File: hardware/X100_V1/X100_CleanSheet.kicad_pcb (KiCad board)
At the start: 4 copper layers, 45 x 45 mm, 205 parts, among them J401 124019772112A, J501 1040310811, J601 SM04B-GHS-TB(LF)(SN), J701 SM06B-GHS-TB(LF)(SN), J702 SM06B-GHS-TB(LF)(SN), J703 SM06B-GHS-TB(LF)(SN), J704 SM04B-GHS-TB(LF)(SN), J801 OUT1 /GND, J802 OUT2 /GND, J803 OUT3 /GND, J804 OUT4 /GND, J805 OUT5 /GND, J806 OUT6 /GND, J807 SWD:1REF2GND3IO4CLK5NRST, J808 BATTERY/bench3S-6S ONLY, J809 CURRENT monitor only, Q101 DMP6023LSS-13, U101 TPS54360BDDAR, U102 AP63203WU-7, U103 TPS7A2033PDBVR, U104 TPS2553DBVR, U201 STM32H743VIT6, U301 BMI088, U302 SPL06-001, U401 TPD2E2U06QDBZRQ1, U402 SN74LVC1G17DBVR, U403 TPD2E2U06QDBZRQ1, U404 TPD2E2U06QDBZRQ1, U601 TCAN3414DR, U801 TMUX1511PWR, Y201 8.000MHz /CL20pF

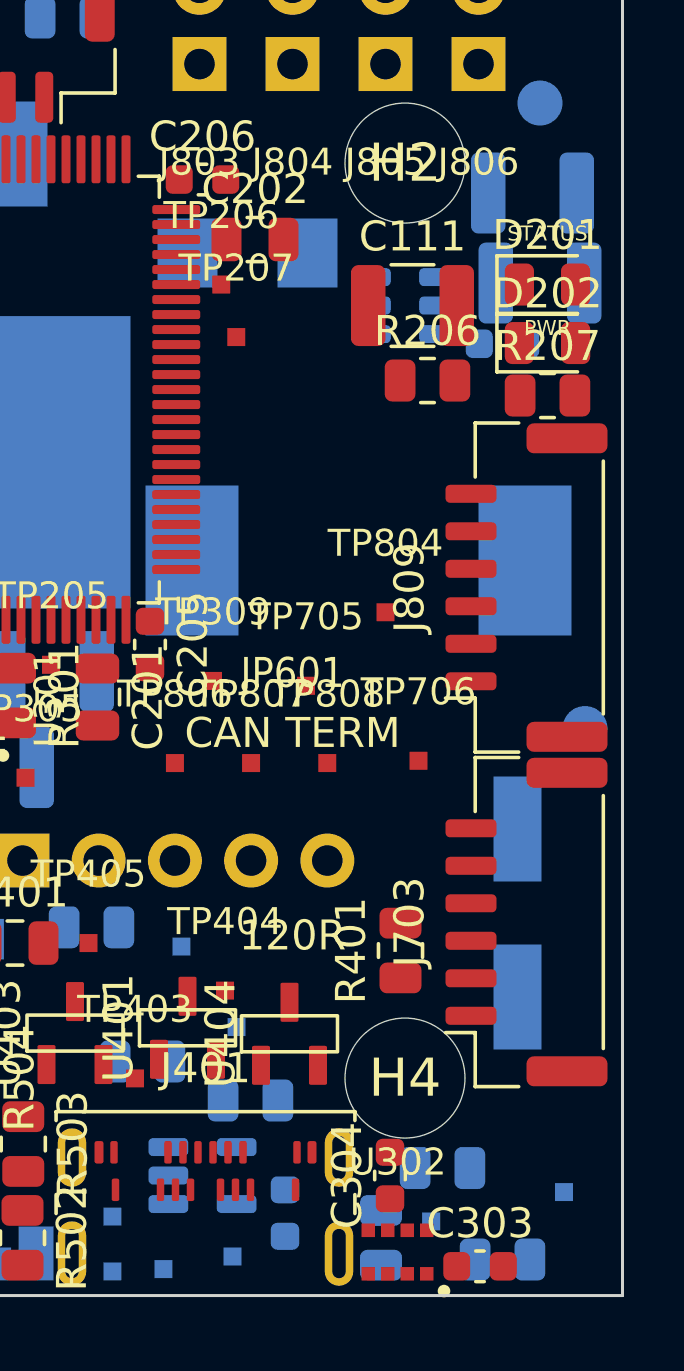
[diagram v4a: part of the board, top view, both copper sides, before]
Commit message: 关闭右侧接口间及J703安装孔净空冲突
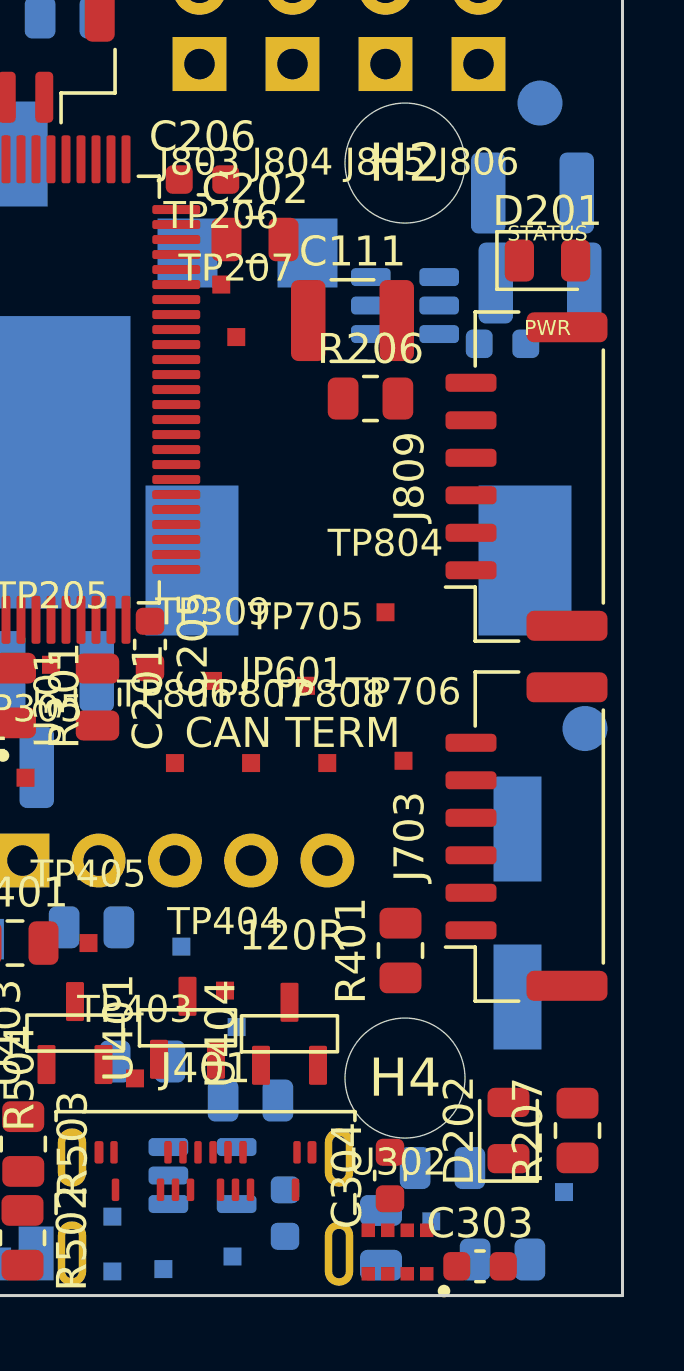
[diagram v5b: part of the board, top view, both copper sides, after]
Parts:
- moved D202 26.3 mm to (118.7, 117.0), turned to 90 degrees
- moved R207 24.5 mm to (121.0, 117.0), turned to 90 degrees
- moved J809 3.70 mm to (119.3, 95.2)
- moved J703 2.85 mm to (119.3, 107.2)
- moved C111 2.06 mm to (113.5, 90.0)
- moved R206 1.99 mm to (114.1, 92.6)
- moved D201 0.80 mm to (120.0, 88.0)
- moved TP706 0.50 mm to (115.2, 104.7)
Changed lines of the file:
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@@
 	(footprint "X100_Physical:Official_LED_SMD_LED_0805_2012Metric"
 		(layer "F.Cu")
-		(at 120 88.8)
+		(at 120 88)
 		(descr "LED SMD 0805 (2012 Metric), square (rectangular) end terminal, IPC-7351 nominal, (Body size source: https://docs.google.com/spreadsheets/d/1BsfQQcO9C6DZCsRaXUlFlo91Tg2WpOkGARC1WS5S8t0/edit?usp=sharing)")
 		(tags "LED")
@@
 	(footprint "X100_Physical:Official_Capacitor_SMD_C_1210_3225Metric"
 		(layer "F.Cu")
-		(at 115.5 89.5)
+		(at 113.5 90)
 		(descr "Capacitor SMD 1210 (3225 Metric), square (rectangular) end terminal, IPC-7351 nominal, (Body size source: IPC-SM-782 page 76, https://www.pcb-3d.com/wordpress/wp-content/uploads/ipc-sm-782a_amendment_1_and_2.pdf)")
 		(tags "capacitor")
@@
 	(footprint "X100_Physical:TP0p6_Inline_NoPaste"
 		(layer "F.Cu")
-		(at 115.7 104.675)
+		(at 115.2 104.675)
 		(descr "Project0.6mm inline probe pad; high speed no long branch; no hole; no paste")
 		(property "Reference" "TP706"
@@
 	(footprint "X100_Physical:Official_Resistor_SMD_R_0805_2012Metric"
 		(layer "F.Cu")
-		(at 120 92.5)
+		(at 121 117 90)
 		(descr "Resistor SMD 0805 (2012 Metric), square (rectangular) end terminal, IPC-7351 nominal, (Body size source: IPC-SM-782 page 72, https://www.pcb-3d.com/wordpress/wp-content/uploads/ipc-sm-782a_amendment_1_and_2.pdf)")
 		(tags "resistor")
 		(property "Reference" "R207"
-			(at 0 -1.65 0)
+			(at 0 -1.65 90)
 			(layer "F.SilkS")
 			(effects
@@
 		)
 		(property "Value" "1.2k PWR current"
-			(at 0 1.65 0)
+			(at 0 1.65 90)
 			(layer "F.Fab")
 			(effects
@@
 		)
 		(property "Datasheet" "https://www.yageogroup.com/component-documentation/download/specsheet/RC0805FR-071K2L"
-			(at 0 0 0)
+			(at 0 0 90)
 			(layer "F.Fab")
 			(hide yes)
@@
 		)
 		(property "Description" ""
-			(at 0 0 0)
+			(at 0 0 90)
 			(layer "F.Fab")
 			(hide yes)
@@
 		)
 		(property "KiLib_Generator" "SMD_2terminal_chip_molded"
-			(at 0 0 0)
+			(at 0 0 90)
 			(layer "F.SilkS")
 			(hide yes)
@@
 		)
 		(property "Manufacturer" "YAGEO"
-			(at 0 0 0)
+			(at 0 0 90)
 			(layer "F.Fab")
 			(hide yes)
@@
 		)
 		(property "MPN" "RC0805FR-071K2L"
-			(at 0 0 0)
+			(at 0 0 90)
 			(layer "F.Fab")
 			(hide yes)
@@
 		)
 		(property "Package" "0805"
-			(at 0 0 0)
+			(at 0 0 90)
 			(layer "F.Fab")
 			(hide yes)
@@
 		)
 		(property "Procurement Policy" "SPECIFICATION_FROZEN_PREFERRED_BOM; PCB01F3 prototype 1.2k authorized"
-			(at 0 0 0)
+			(at 0 0 90)
 			(layer "F.Fab")
 			(hide yes)
@@
 		)
 		(property "Specification Value" "1.2k ohm"
-			(at 0 0 0)
+			(at 0 0 90)
 			(layer "F.Fab")
 			(hide yes)
@@
 		)
 		(property "Tolerance" "1%; TCR<=100ppm/C"
-			(at 0 0 0)
+			(at 0 0 90)
 			(layer "F.Fab")
 			(hide yes)
@@
 		)
 		(property "Dielectric" "N/A"
-			(at 0 0 0)
+			(at 0 0 90)
 			(layer "F.Fab")
 			(hide yes)
@@
 		)
 		(property "Voltage Rating" ">=100V"
-			(at 0 0 0)
+			(at 0 0 90)
 			(layer "F.Fab")
 			(hide yes)
@@
 		)
 		(property "Power Rating" ">=0.125W"
-			(at 0 0 0)
+			(at 0 0 90)
 			(layer "F.Fab")
 			(hide yes)
@@
 		)
 		(property "LCSC" "C114526"
-			(at 0 0 0)
+			(at 0 0 90)
 			(layer "F.Fab")
 			(hide yes)
@@
 		)
 		(fp_text user "${REFERENCE}"
-			(at 0 0 0)
+			(at 0 0 90)
 			(layer "F.Fab")
 			(effects
@@
 		)
 		(pad "1" smd roundrect
-			(at -0.9125 0)
+			(at -0.9125 0 90)
 			(size 1.025 1.4)
 			(layers "F.Cu" "F.Mask" "F.Paste")
@@
 		)
 		(pad "2" smd roundrect
-			(at 0.9125 0)
+			(at 0.9125 0 90)
 			(size 1.025 1.4)
 			(layers "F.Cu" "F.Mask" "F.Paste")
@@
 	(footprint "X100_Physical:Official_Connector_JST_JST_GH_SM06B-GHS-TB_1x06-1MP_P1.25mm_Horizontal"
 		(layer "F.Cu")
-		(at 119.3 98.899999 90)
+		(at 119.3 95.2 90)
 		(descr "JST GH series connector, SM06B-GHS-TB (http://www.jst-mfg.com/product/pdf/eng/eGH.pdf)")
 		(tags "connector JST GH horizontal")
@@
 	(footprint "X100_Physical:Official_Connector_JST_JST_GH_SM06B-GHS-TB_1x06-1MP_P1.25mm_Horizontal"
 		(layer "F.Cu")
-		(at 119.3 110.05 90)
+		(at 119.3 107.2 90)
 		(descr "JST GH series connector, SM06B-GHS-TB (http://www.jst-mfg.com/product/pdf/eng/eGH.pdf)")
 		(tags "connector JST GH horizontal")
@@
 	(footprint "X100_Physical:Official_LED_SMD_LED_0805_2012Metric"
 		(layer "F.Cu")
-		(at 120 90.75)
+		(at 118.7 117 90)
 		(descr "LED SMD 0805 (2012 Metric), square (rectangular) end terminal, IPC-7351 nominal, (Body size source: https://docs.google.com/spreadsheets/d/1BsfQQcO9C6DZCsRaXUlFlo91Tg2WpOkGARC1WS5S8t0/edit?usp=sharing)")
 		(tags "LED")
 		(property "Reference" "D202"
-			(at 0 -1.65 0)
+			(at 0 -1.65 90)
 			(layer "F.SilkS")
 			(effects
@@
 		)
 		(property "Value" "GREEN; 3V3_MCU_PRESENT"
-			(at 0 1.65 0)
+			(at 0 1.65 90)
 			(layer "F.Fab")
 			(effects
@@
 		)
 		(property "Datasheet" "https://optoelectronics.liteon.com/upload/download/DS22-2000-003/LTST-C170GKT.pdf"
-			(at 0 0 0)
+			(at 0 0 90)
 			(layer "F.Fab")
 			(hide yes)
@@
 		)
 		(property "Description" ""
-			(at 0 0 0)
+			(at 0 0 90)
 			(layer "F.Fab")
 			(hide yes)
@@
 		)
 		(property "KiLib_Generator" "SMD_2terminal_chip_molded"
-			(at 0 0 0)
+			(at 0 0 90)
 			(layer "F.SilkS")
 			(hide yes)
@@
 		)
 		(property "Manufacturer" "Lite-On"
-			(at 0 0 0)
+			(at 0 0 90)
 			(layer "F.Fab")
 			(hide yes)
@@
 		)
 		(property "MPN" "LTST-C170GKT"
-			(at 0 0 0)
+			(at 0 0 90)
 			(layer "F.Fab")
 			(hide yes)
@@
 		)
 		(property "Package" "0805 LED"
-			(at 0 0 0)
+			(at 0 0 90)
 			(layer "F.Fab")
 			(hide yes)
@@
 		)
 		(property "Procurement Policy" "EXACT_MPN_AUTHORIZED_PCB01F3; same LED as D201; not ordered"
-			(at 0 0 0)
+			(at 0 0 90)
 			(layer "F.Fab")
 			(hide yes)
@@
 		)
 		(property "LCSC" "C125090"
-			(at 0 0 0)
+			(at 0 0 90)
 			(layer "F.Fab")
 			(hide yes)
@@
 		(duplicate_pad_numbers_are_jumpers no)
 		(fp_line
-			(start -1.685 -0.96)
-			(end -1.685 0.96)
+			(start 1 -0.96)
+			(end -1.685 -0.96)
 			(stroke
 				(width 0.12)
@@
 		)
 		(fp_line
-			(start -1.685 0.96)
-			(end 1 0.96)
+			(start -1.685 -0.96)
+			(end -1.685 0.96)
 			(stroke
 				(width 0.12)
@@
 		)
 		(fp_line
-			(start 1 -0.96)
-			(end -1.685 -0.96)
+			(start -1.685 0.96)
+			(end 1 0.96)
 			(stroke
 				(width 0.12)
@@
 		)
 		(fp_line
-			(start -1 -0.3)
-			(end -1 0.6)
+			(start 1 -0.6)
+			(end -0.7 -0.6)
 			(stroke
 				(width 0.1)
@@
 		)
 		(fp_line
-			(start -1 0.6)
-			(end 1 0.6)
+			(start -0.7 -0.6)
+			(end -1 -0.3)
 			(stroke
 				(width 0.1)
@@
 		)
 		(fp_line
-			(start -0.7 -0.6)
-			(end -1 -0.3)
+			(start -1 -0.3)
+			(end -1 0.6)
 			(stroke
 				(width 0.1)
@@
 		)
 		(fp_line
-			(start 1 -0.6)
-			(end -0.7 -0.6)
+			(start 1 0.6)
+			(end 1 -0.6)
 			(stroke
 				(width 0.1)
@@
 		)
 		(fp_line
-			(start 1 0.6)
-			(end 1 -0.6)
+			(start -1 0.6)
+			(end 1 0.6)
 			(stroke
 				(width 0.1)
@@
 		)
 		(fp_text user "${REFERENCE}"
-			(at 0 0 0)
+			(at 0 0 90)
 			(layer "F.Fab")
 			(effects
@@
 		)
 		(pad "1" smd roundrect
-			(at -0.9375 0)
+			(at -0.9375 0 90)
 			(size 0.975 1.4)
 			(layers "F.Cu" "F.Mask" "F.Paste")
@@
 		)
 		(pad "2" smd roundrect
-			(at 0.9375 0)
+			(at 0.9375 0 90)
 			(size 0.975 1.4)
 			(layers "F.Cu" "F.Mask" "F.Paste")
@@
 	(footprint "X100_Physical:Official_Resistor_SMD_R_0805_2012Metric"
 		(layer "F.Cu")
-		(at 116 92)
+		(at 114.1 92.6)
 		(descr "Resistor SMD 0805 (2012 Metric), square (rectangular) end terminal, IPC-7351 nominal, (Body size source: IPC-SM-782 page 72, https://www.pcb-3d.com/wordpress/wp-content/uploads/ipc-sm-782a_amendment_1_and_2.pdf)")
 		(tags "resistor")

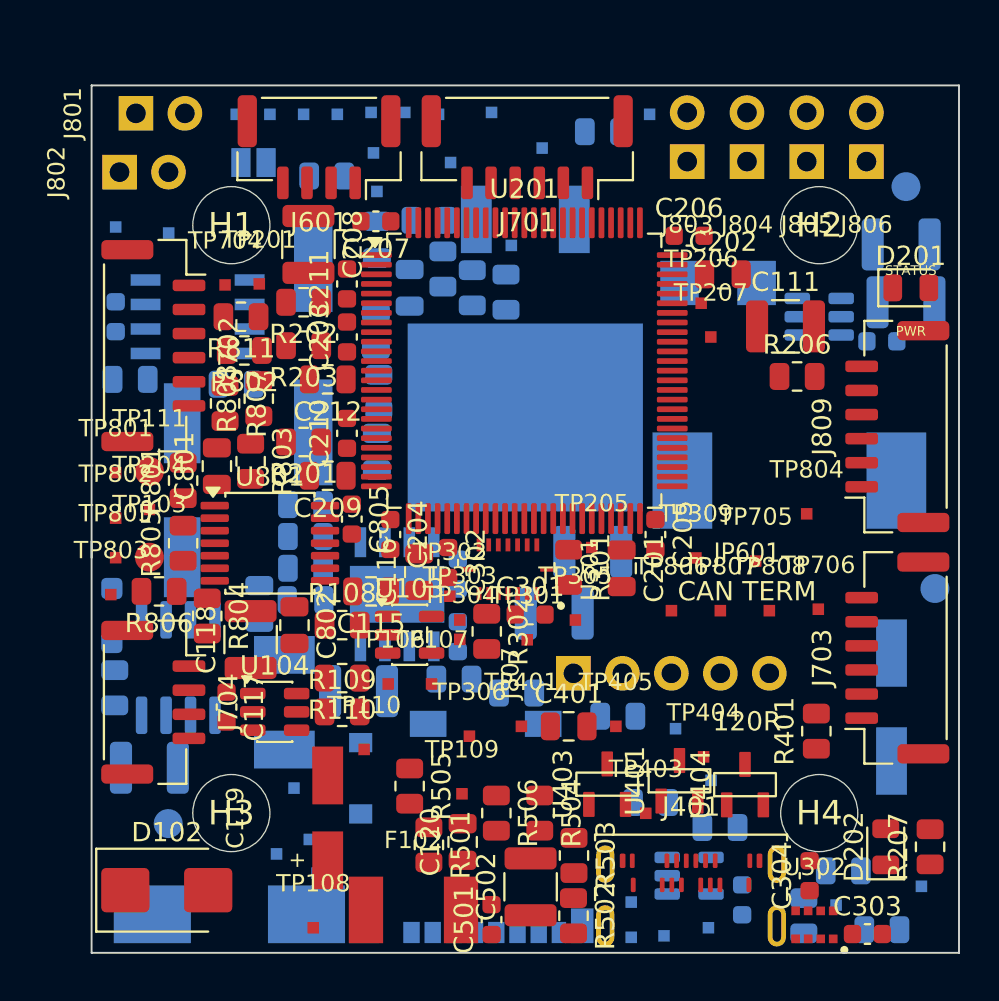
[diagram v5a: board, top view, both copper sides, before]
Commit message: 消除45对测试点及阻容装配庭院冲突
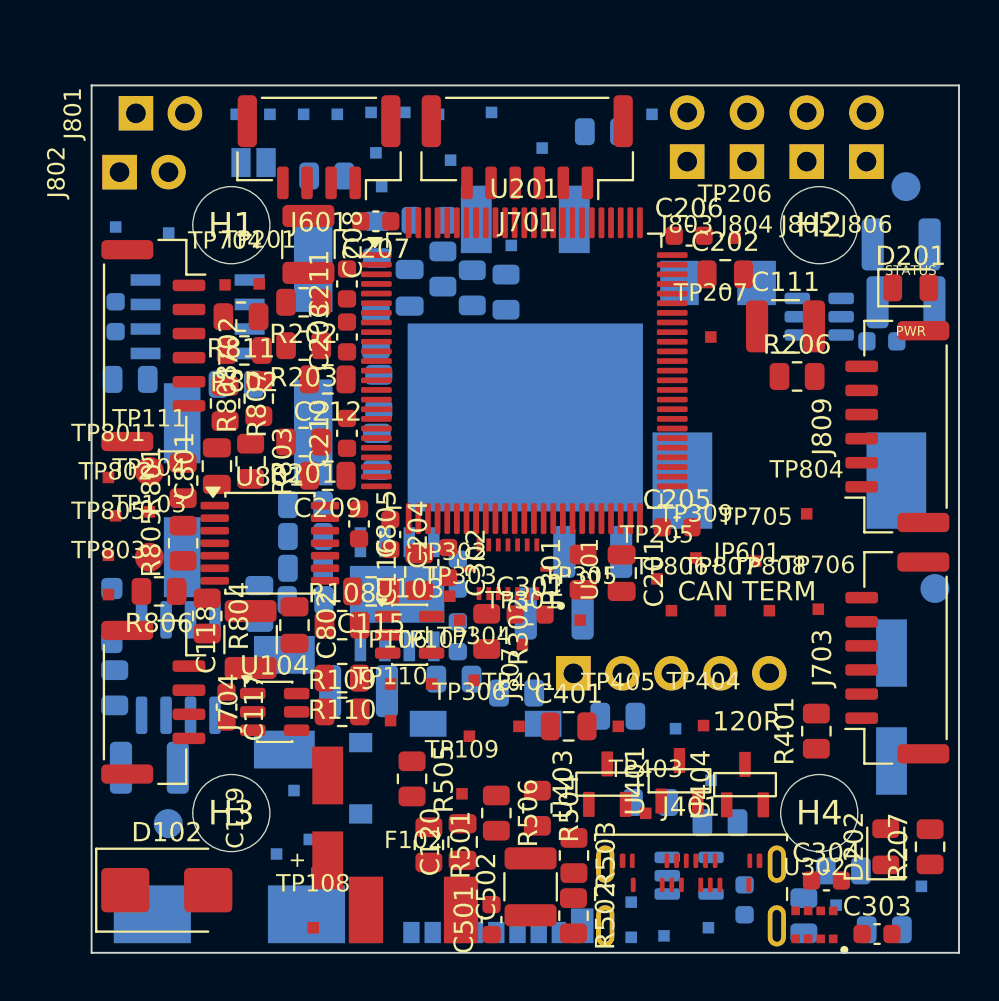
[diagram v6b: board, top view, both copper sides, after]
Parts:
- moved TP206 3.80 mm to (110.9, 85.4)
- moved TP205 3.75 mm to (106.8, 103.1)
- moved TP304 2.25 mm to (97.3, 108.4)
- moved TP110 2.03 mm to (93.0, 110.5)
- moved TP404 1.62 mm to (109.2, 110.7)
- moved C205 1.19 mm to (107.9, 100.4), turned to 0 degrees
- moved C304 0.91 mm to (115.6, 118.8), turned to 0 degrees
- moved R301 0.79 mm to (103.0, 102.8), turned to 90 degrees
- moved C303 0.50 mm to (118.2, 121.5)
- moved C805 0.45 mm to (91.4, 100.2)
- moved TP801 0.45 mm to (78.4, 97.8)
- moved R505 0.40 mm to (94.1, 113.5)
- moved TP805 0.40 mm to (78.4, 101.9)
- moved TP208 0.35 mm to (92.5, 82.8)
- moved TP301 0.35 mm to (99.8, 106.5)
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
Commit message: 调整MCU储能电容与SWD排针释放局部空间
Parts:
- moved TP111 34.6 mm to (114.8, 102.5)
- moved C208 26.8 mm to (111.8, 99.5), turned to 0 degrees
- moved TP103 13.7 mm to (79.2, 115.6)
- moved TP305 3.37 mm to (101.1, 108.1)
- moved J807 1.38 mm to (103.7, 107.4)
- moved TP804 0.30 mm to (114.9, 99.7)
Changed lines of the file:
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@@
 	(footprint "X100_Physical:TP1p5_NoPaste"
 		(layer "F.Cu")
-		(at 80.5 101.975)
+		(at 79.25 115.625)
 		(descr "Project1.5mm round accessible top test pad; no hole; no paste")
 		(property "Reference" "TP103"
@@
 	(footprint "X100_Physical:TP0p6_Inline_NoPaste"
 		(layer "F.Cu")
-		(at 102.85 105.238)
+		(at 101.1 108.113)
 		(descr "Project0.6mm inline probe pad; high speed no long branch; no hole; no paste")
 		(property "Reference" "TP305"
@@
 	(footprint "X100_Physical:Samtec_TSW10507GS_1x5_P2p54"
 		(layer "F.Cu")
-		(at 102.5 108 90)
+		(at 103.725 107.375 90)
 		(descr "Samtec exact TSW print/footprint;0.635square post;1.02mm finished drill")
 		(property "Reference" "J807"
@@
 	(footprint "X100_Physical:TP0p6_Inline_NoPaste"
 		(layer "F.Cu")
-		(at 114.6 99.725)
+		(at 114.9 99.725)
 		(descr "Project0.6mm inline probe pad; high speed no long branch; no hole; no paste")
 		(property "Reference" "TP804"
@@
 	(footprint "X100_Physical:Official_Capacitor_SMD_C_1210_3225Metric"
 		(layer "F.Cu")
-		(at 88.75 85.75 -90)
+		(at 111.75 99.5)
 		(descr "Capacitor SMD 1210 (3225 Metric), square (rectangular) end terminal, IPC-7351 nominal, (Body size source: IPC-SM-782 page 76, https://www.pcb-3d.com/wordpress/wp-content/uploads/ipc-sm-782a_amendment_1_and_2.pdf)")
 		(tags "capacitor")
 		(property "Reference" "C208"
-			(at 0 -2.3 270)
+			(at 0 -2.3 0)
 			(layer "F.SilkS")
 			(effects
@@
 		)
 		(property "Value" "10u /50V MCU bulk >=4.7u effective"
-			(at 0 2.3 270)
+			(at 0 2.3 0)
 			(layer "F.Fab")
 			(effects
@@
 		)
 		(property "Datasheet" "https://www.yageogroup.com/component-documentation/download/specsheet/C1210C106K5RACTU"
-			(at 0 0 270)
+			(at 0 0 0)
 			(layer "F.Fab")
 			(hide yes)
@@
 		)
 		(property "Description" ""
-			(at 0 0 270)
+			(at 0 0 0)
 			(layer "F.Fab")
 			(hide yes)
@@
 		)
 		(property "KiLib_Generator" "SMD_2terminal_chip_molded"
-			(at 0 0 270)
+			(at 0 0 0)
 			(layer "F.SilkS")
 			(hide yes)
@@
 		)
 		(property "Manufacturer" "KEMET"
-			(at 0 0 270)
+			(at 0 0 0)
 			(unlocked yes)
 			(layer "F.Fab")
@@
 		)
 		(property "MPN" "C1210C106K5RACTU"
-			(at 0 0 270)
+			(at 0 0 0)
 			(unlocked yes)
 			(layer "F.Fab")
@@
 		)
 		(property "Package" "1210"
-			(at 0 0 270)
+			(at 0 0 0)
 			(unlocked yes)
 			(layer "F.Fab")
@@
 		)
 		(property "Procurement Policy" "SPECIFICATION_FROZEN_PREFERRED_BOM"
-			(at 0 0 270)
+			(at 0 0 0)
 			(unlocked yes)
 			(layer "F.Fab")
@@
 		)
 		(property "Specification Value" "10uF"
-			(at 0 0 270)
+			(at 0 0 0)
 			(unlocked yes)
 			(layer "F.Fab")
@@
 		)
 		(property "Tolerance" "10%"
-			(at 0 0 270)
+			(at 0 0 0)
 			(unlocked yes)
 			(layer "F.Fab")
@@
 		)
 		(property "Dielectric" "X7R"
-			(at 0 0 270)
+			(at 0 0 0)
 			(unlocked yes)
 			(layer "F.Fab")
@@
 		)
 		(property "Voltage Rating" ">=50V"
-			(at 0 0 270)
+			(at 0 0 0)
 			(unlocked yes)
 			(layer "F.Fab")
@@
 		)
 		(property "Power Rating" "N/A"
-			(at 0 0 270)
+			(at 0 0 0)
 			(unlocked yes)
 			(layer "F.Fab")
@@
 		(duplicate_pad_numbers_are_jumpers no)
 		(fp_line
-			(start -0.711252 1.36)
-			(end 0.711252 1.36)
+			(start -0.711252 -1.36)
+			(end 0.711252 -1.36)
 			(stroke
 				(width 0.12)
@@
 		)
 		(fp_line
-			(start -0.711252 -1.36)
-			(end 0.711252 -1.36)
+			(start -0.711252 1.36)
+			(end 0.711252 1.36)
 			(stroke
 				(width 0.12)
@@
 		)
 		(fp_text user "${REFERENCE}"
-			(at 0 0 270)
+			(at 0 0 0)
 			(layer "F.Fab")
 			(effects
@@
 		)
 		(pad "1" smd roundrect
-			(at -1.475 0 270)
+			(at -1.475 0)
 			(size 1.15 2.7)
 			(layers "F.Cu" "F.Mask" "F.Paste")
@@
 		)
 		(pad "2" smd roundrect
-			(at 1.475 0 270)
+			(at 1.475 0)
 			(size 1.15 2.7)
 			(layers "F.Cu" "F.Mask" "F.Paste")
@@
 	(footprint "X100_Physical:TP1p5_NoPaste"
 		(layer "F.Cu")
-		(at 80.5 97.525)
+		(at 114.75 102.45)
 		(descr "Project1.5mm round accessible top test pad; no hole; no paste")
 		(property "Reference" "TP111"
